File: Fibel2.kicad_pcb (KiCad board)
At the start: 4 copper layers, 210 x 148 mm, 464 parts, among them IC1 ICS-43434, IC2 ICS-43434, IC3 ICS-43434, IC4 ICS-43434, IC5 TXB0108RGYR, IC6 TXB0108RGYR, IC7 TXB0108RGYR, IC9 TXB0108RGYR, J1 Raspi_Header, J1201 Orin Nano, J2 Raspi_Header, J3 Conn_01x02, J301 Conn_01x02, J302 Conn_01x02, J303 Conn_01x02, J4 ED060SC4, J401 USB-C_USB4105-GF-A, J402 Conn_USB-C_WE_632723300011, J5 ED060SC7, J8 SJ2-35954D-SMT-TR, J9 Conn_01x02, J901 Bus_M.2_2199230-6, J902 Bus_M.2_1-2199230-6, Q1 PJE138K_2, Q2 PJE138K_2, Q301 CSD17581Q3A, Q302 CSD17581Q3A, Q303 CSD17581Q3A, Q304 CSD17581Q3A, U1 TPS651851RSLT, U2 74LVC2G14_SOT457, U202 TLV75733PDBV, U204 TPS56428DDA, U205 TPS56428DDA, U3 TPS65988DHRSHR, U301 BQ25798RQMR, U4 ESP32-S3-WROOM-1U, U403 FT230X_QFN, U404 AP22615_1, U405 TUSB1046-DCIRNQ, U406 AP22615_1, U407 TPD4E05U06QDQARQ1, U408 TPD4E05U06QDQARQ1, U409 W25Q80DV_USON, U410 TPD4E05U06QDQARQ1, U411 TPD4E05U06QDQARQ1, U412 TPD4E05U06QDQARQ1, U5 TLV75733PDBV, U6 74LVC1G175_SOT457, U7 TLV75733PDBV, U701 WM8960CGEFL, U8 PCAL6408A_VQFN, X701 24MHz 306020014, Y1 ECS-327ATQ2520MV-32.786K

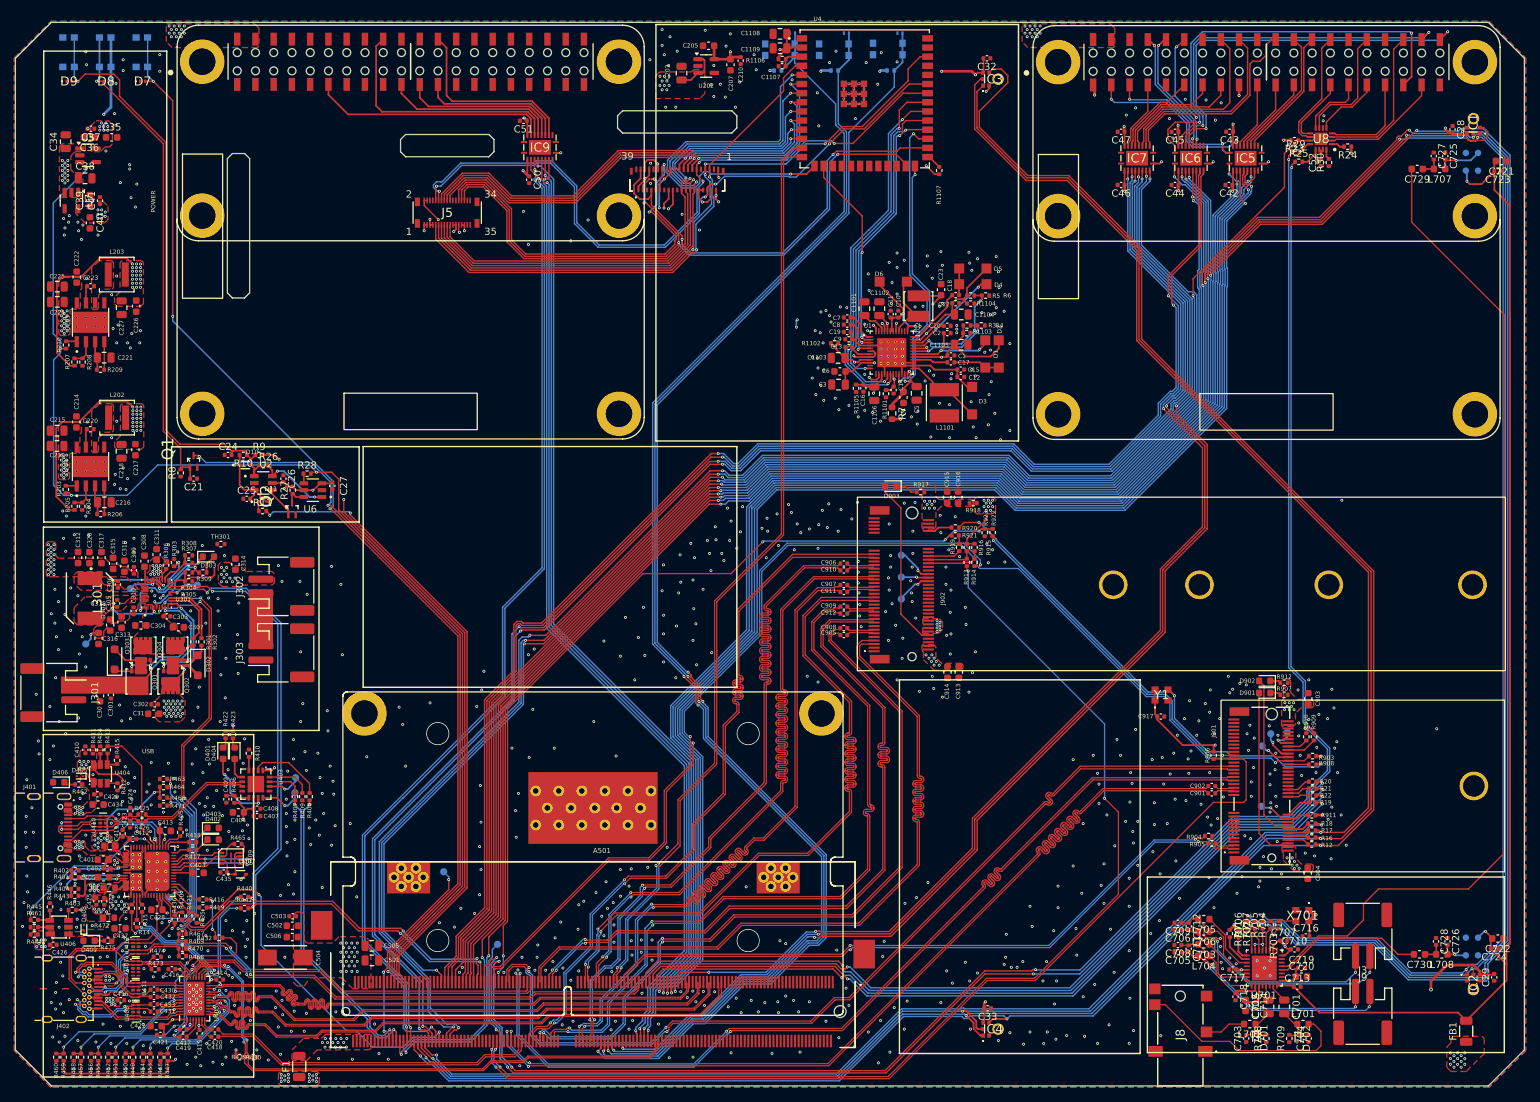
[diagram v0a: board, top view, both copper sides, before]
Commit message: finished routing, sanity check and prep fabrication files next
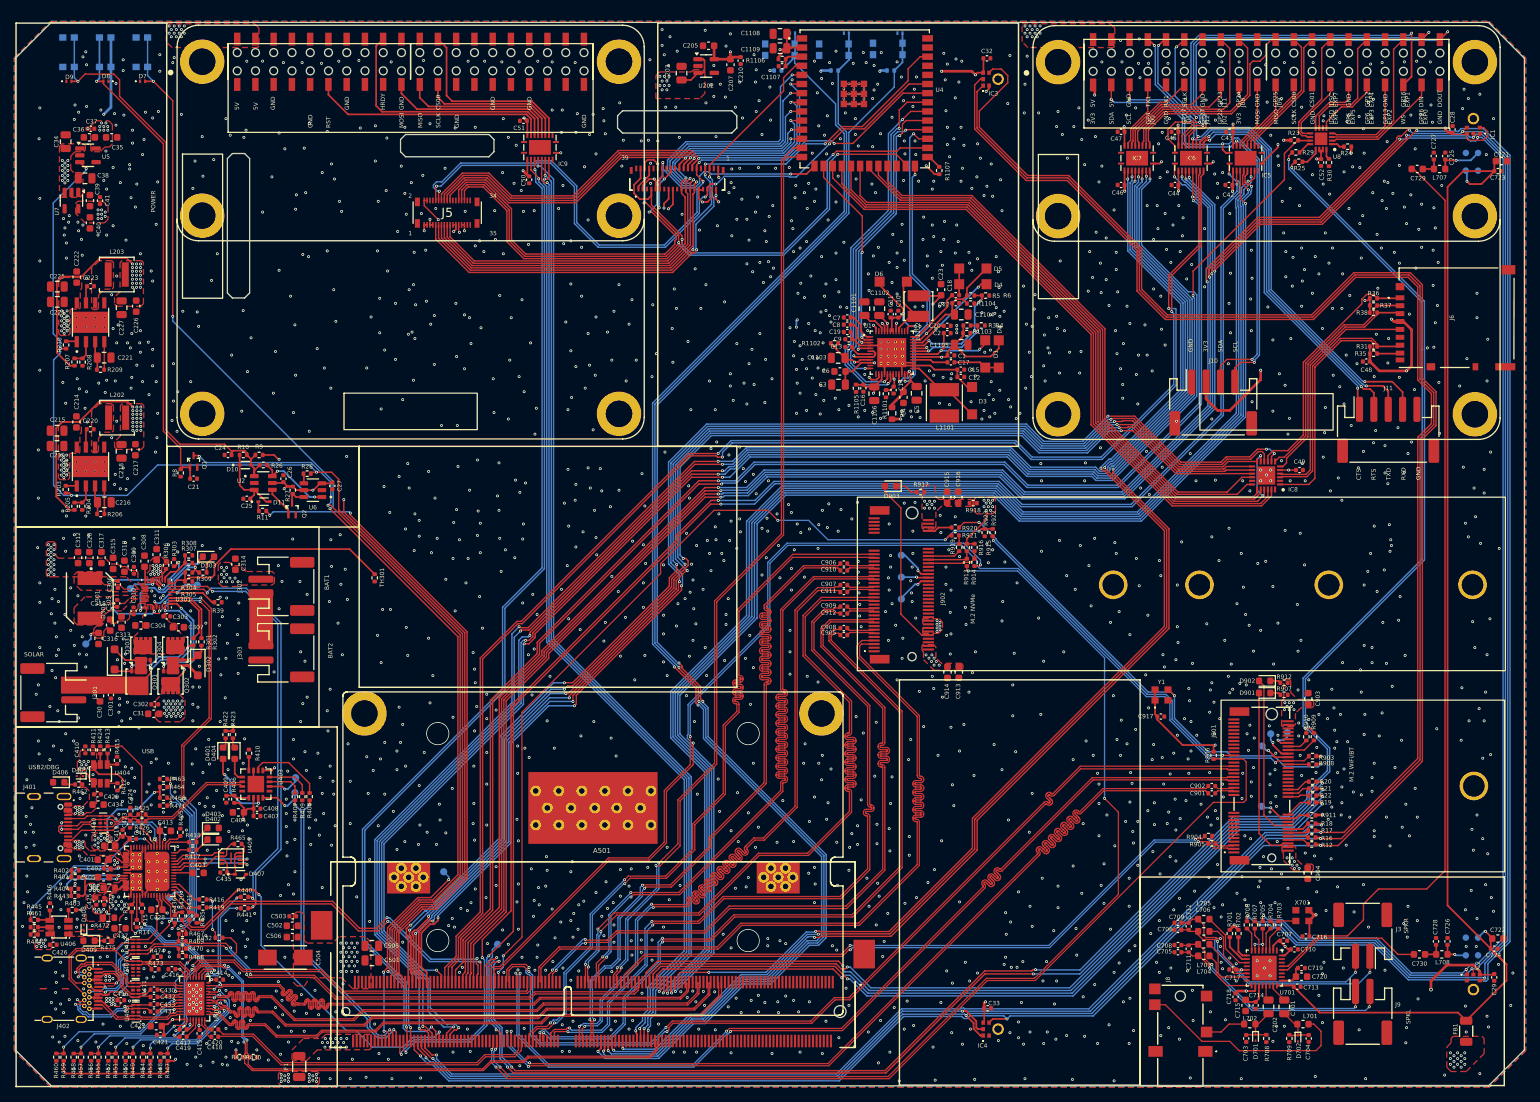
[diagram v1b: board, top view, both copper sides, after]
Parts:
- added C48: 100nF, Capacitor_SMD:C_0402_1005Metric, F.Cu at (203.0, 62.2)
- added C49: 100nF, Capacitor_SMD:C_0402_1005Metric, F.Cu at (193.7, 77.3)
- added IC8: TS3A27518ERTWR, Fibel2:QFN50P400X400X80-25N, F.Cu at (189.1, 78.0)
- added J10: Conn_01x04, Connector_JST:JST_PH_S4B-PH-SM4-TB_1x04-1MP_P2.00mm_Horizontal, F.Cu at (181.7, 67.9)
- added J11: Conn_01x05, Connector_JST:JST_PH_S5B-PH-SM4-TB_1x05-1MP_P2.00mm_Horizontal, F.Cu at (206.1, 71.7)
- added J6: DM3AT-SF-PEJM5_40_, Fibel2:DM3ATSFPEJM540, F.Cu at (208.3, 53.3)
- added R31: 10K, Resistor_SMD:R_0402_1005Metric, F.Cu at (204.0, 60.1)
- added R35: 10K, Resistor_SMD:R_0402_1005Metric, F.Cu at (204.0, 61.1)
- added R36: 10K, Resistor_SMD:R_0402_1005Metric, F.Cu at (204.0, 53.4)
- added R37: 10K, Resistor_SMD:R_0402_1005Metric, F.Cu at (204.0, 54.4)
- added R38: 10K, Resistor_SMD:R_0402_1005Metric, F.Cu at (204.0, 55.4)
- added R39: 10K, Resistor_SMD:R_0402_1005Metric, F.Cu at (43.2, 95.7)
- moved TH301 21.9 mm to (65.0, 92.3), turned to -90 degrees
- moved J4 0.12 mm to (107.1, 36.6)
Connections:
- J1201 pad 219: unconnected-(J1201D-PCIE2_RST-Pad219) -> ORIN_SDMMC_DAT0
- J1201 pad 221: unconnected-(J1201D-PCIE2_CLKREQ-Pad221) -> ORIN_SDMMC_DAT1
- J1201 pad 223: unconnected-(J1201D-PCIE3_RST-Pad223) -> ORIN_SDMMC_DAT2
- J1201 pad 225: unconnected-(J1201D-PCIE3_CLKREQ-Pad225) -> ORIN_SDMMC_DAT3
- J1201 pad 227: unconnected-(J1201D-PCIE3_CLK_N-Pad227) -> ORIN_SDMMC_CMD
- J1201 pad 229: unconnected-(J1201D-PCIE3_CLK_P-Pad229) -> ORIN_SDMMC_CLK
- U4 pad 17: unconnected-(U4-IO9-Pad17) -> EPD_SDMMC_DAT1
- U4 pad 18: unconnected-(U4-IO10-Pad18) -> EPD_SDMMC_DAT0
- U4 pad 19: unconnected-(U4-IO11-Pad19) -> EMMC_IN
- U4 pad 20: unconnected-(U4-IO12-Pad20) -> EPD_SDMMC_CLK
- U4 pad 21: unconnected-(U4-IO13-Pad21) -> EPD_SDMMC_DAT2
- U4 pad 22: unconnected-(U4-IO14-Pad22) -> EPD_SDMMC_CMD
- U4 pad 23: unconnected-(U4-IO21-Pad23) -> EPD_SDMMC_DAT3
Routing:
- net ORIN_SDMMC_DAT1: track 0.00 -> 184.3 mm, vias 0 -> 6
- net ORIN_SDMMC_DAT0: track 0.00 -> 182.4 mm, vias 0 -> 4
- net ORIN_SDMMC_CLK: track 0.00 -> 178.5 mm, vias 0 -> 4
- net ORIN_SDMMC_DAT2: track 0.00 -> 177.5 mm, vias 0 -> 4
- net ORIN_SDMMC_CMD: track 0.00 -> 176.7 mm, vias 0 -> 4
- net ORIN_SDMMC_DAT3: track 0.00 -> 176.3 mm, vias 0 -> 4
- net EPD_3V3: track 162.3 -> 297.1 mm, vias 8 -> 14
- net EMMC_IN: track 0.00 -> 94.4 mm, vias 0 -> 2
- net EPD_SDMMC_DAT1: track 0.00 -> 90.5 mm
- net EPD_SDMMC_DAT0: track 0.00 -> 88.9 mm
- net EPD_SDMMC_CLK: track 0.00 -> 85.5 mm
- net EPD_SDMMC_DAT2: track 0.00 -> 81.4 mm
- net EPD_SDMMC_CMD: track 0.00 -> 79.6 mm
- net EPD_SDMMC_DAT3: track 0.00 -> 79.0 mm
- net UART1_3V3_RXD: track 17.5 -> 75.7 mm, vias 2 -> 3
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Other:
- board text added: "3V3"
- board text added: "5V"
- board text added: "BAT1"
- board text added: "BAT2"
- board text added: "BOOT"
- board text added: "CS00"
- board text added: "CS01"
- board text added: "CTS"
- board text added: "DIN"
- board text added: "DOUT"
- board text added: "EXP0"
- board text added: "EXP1"
- board text added: "EXP2"
- board text added: "EXP3"
- board text added: "EXP4"
- board text added: "EXP5"
- board text added: "EXP6"
- board text added: "EXP7"
- board text added: "GND"
- board text added: "GP12"
- board text added: "GP13"
- board text added: "GP16"
- board text added: "GP17"
- board text added: "GP22"
- board text added: "GP23"
- board text added: "GP24"
- board text added: "GP25"
- board text added: "GP26"
- board text added: "GP27"
- board text added: "GP4"
- board text added: "GP5"
- board text added: "GP6"
- board text added: "HRDY"
- board text added: "IDSC"
- board text added: "IDSD"
- board text added: "J00"
- board text added: "J01"
- board text added: "J02"
- board text added: "J03"
- board text added: "J05"
- board text added: "J06"
- board text added: "J08"
- board text added: "J09"
- board text added: "J11"
- board text added: "J12"
- board text added: "M.2 NVMe"
- board text added: "M.2 WiFi/BT"
- board text added: "MISO"
- board text added: "MOSI"
- board text added: "RECOVERY"
- board text added: "RESET"
- board text added: "RST"
- board text added: "RTS"
- board text added: "RX1"
- board text added: "RXD"
- board text added: "SCL"
- board text added: "SCLK"
- board text added: "SDA"
- board text added: "SOLAR"
- board text added: "SPKL"
- board text added: "SPKR"
- board text added: "TX1"
- board text added: "TXD"
- board text added: "USB2/DBG"
- board text added: "WS"
